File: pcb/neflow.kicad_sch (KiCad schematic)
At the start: 6 parts, among them Q1 IRLML2502, U1 MAX31855SASA, U2 MAX31855SASA, U3 LM1117DT-3.3

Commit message: WIP: Schematic rev0 almost done
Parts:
- added Brd1: SSD1306, SSD1306:128x64OLED, symbol SSD1306-128x64_OLED:SSD1306
- added C10, C12, C13, C2, C3, C5, C6, C7, C8, C9: 10uF, symbol Device:C_Small
- added C11: 100nF, symbol Device:C_Polarized_Small
- added C4: 10nF, symbol Device:C_Small
- added D1, D2, D3: 1N4148W, symbol Device:D_Small
- added FB2, FB3, FB4: BLM18PG471, Resistor_SMD:R_0603_1608Metric, symbol Device:FerriteBead_Small
- added J1, J2, J5: Conn_01x02_Socket, symbol Connector:Conn_01x02_Socket
- added J3: SSR0, symbol Connector:Conn_01x02_Socket
- added J4: SSR1, symbol Connector:Conn_01x02_Socket
- added J7: FAN1, symbol Connector:Conn_01x02_Socket
- added J8: FAN0, symbol Connector:Conn_01x02_Socket
- added JP1: VSel0, symbol Jumper:SolderJumper_3_Open
- added JP2: SolderJumper_3_Open, symbol Jumper:SolderJumper_3_Open
- added LS1: Speaker, symbol Device:Speaker
- added PS1: HLK-PM01, Converter_ACDC:Converter_ACDC_HiLink_HLK-PMxx, symbol Converter_ACDC:HLK-PM01
- added Q2, Q3, Q4, Q5: IRLML2502, Package_TO_SOT_SMD:SOT-23, symbol Transistor_FET:IRLML2060
- added R1: R_Small, symbol Device:R_Small
- added R10, R2, R3, R4, R5, R6, R7, R8, R9: 10K, symbol Device:R_Small
- added SW1, SW2, SW3, SW4: SW_Push, symbol Switch:SW_Push
- C1: value 0.01uF -> 10nF; LCSC (none) -> C57112
- FB1: LCSC (none) -> C97853
- Q1: LCSC (none) -> C2589
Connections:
- net GND: now reaches U3.1 (GND)
- net GND: now also Q1.2 (S), U1.1 (GND), U2.1 (GND), Brd1.1 (GND), C10.2, C11.2, C12.2, C13.2, C2.2, C3.2, C5.2, C6.2, C7.2, C8.2, C9.2, JP1.3 (B), JP2.3 (B), Q2.2 (S), Q3.2 (S), Q4.2 (S), Q5.2 (S), R2.1, R3.1, R4.1, R5.1, R6.1, SW1.1, SW2.1, SW3.1, SW4.1
- net +3.3V: now reaches U3.2 (VO)
- net +3.3V: now also U1.4 (V_CC), U2.4 (V_CC), Brd1.2 (VCC), C13.1, C2.1, C3.1, C5.1, C6.1, C7.1, C8.1, D3.1 (K), LS1.1, R10.2, R7.2, R8.2, R9.2
- net +5V: now reaches U3.3 (VI)
- net +5V: now also C10.1, C11.1, C12.1, C9.1, D1.1 (K), D2.1 (K), J3.1 (Pin_1), J4.1 (Pin_1), J7.1 (Pin_1), J8.1 (Pin_1), JP1.1 (A), JP2.1 (A)
- net TC1-: now reaches U2.2 (T-)
- net TC1-: now also C4.2, FB4.2
- net TC1+: now reaches U2.3 (T+)
- net TC1+: now also C4.1, FB3.1
- net SSR0: now reaches Q1.1 (G)
- net SSR0: now also R2.2
- net SSR0B: now reaches Q1.3 (D)
- net SSR0B: now also J3.2 (Pin_2)
- net TC0+: now reaches C1.1
- net TC0+: now also U1.3 (T+), FB2.1
- net TC0-: now reaches C1.2
- net TC0-: now also FB1.2, U1.2 (T-)
- net T0-: now reaches FB1.1
- net T0-: now also J1.1 (Pin_1)
- new net: J5.1 (Pin_1), PS1.1 (AC/L)
- new net: J5.2 (Pin_2), PS1.2 (AC/N)
- new net: JP2.2 (C), PS1.3 (-Vout)
- new net: JP1.2 (C), PS1.4 (+Vout)
- new net BTN0: R7.1, SW1.2
- new net BTN1: R8.1, SW2.2
- new net BTN2: R9.1, SW3.2
- new net BTN3: R10.1, SW4.2
- new net FAN0: Q4.1 (G), R5.2
- new net FAN0B: D1.2 (A), J8.2 (Pin_2), Q4.3 (D)
- new net FAN1: Q3.1 (G), R4.2
- new net FAN1B: D2.2 (A), J7.2 (Pin_2), Q3.3 (D)
- new net SPK: Q5.1 (G), R6.2
- new net SPKB: D3.2 (A), LS1.2, Q5.3 (D)
- new net SSR1: Q2.1 (G), R3.2
- new net SSR1B: J4.2 (Pin_2), Q2.3 (D)
- new net T0+: FB2.2, J1.2 (Pin_2)
- new net T1+: FB3.2, J2.2 (Pin_2)
- new net T1-: FB4.1, J2.1 (Pin_1)
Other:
- note added: "3.3V Power Supply"
- note added: "Power Supply: AC -> 5v"
- moved on the sheet: C1, FB1, Q1, U1, U3

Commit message: WIP: Adding button footprint
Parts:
- LS1: footprint (none) -> Library:PassiveBuzzerSMD_JiangsuHuaneng_MLT-5030
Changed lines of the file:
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@@
       (effects (font (size 1.27 1.27)) (justify left))
     )
-    (property "Footprint" "" (at 198.12 157.48 0)
+    (property "Footprint" "Library:PassiveBuzzerSMD_JiangsuHuaneng_MLT-5030" (at 198.12 157.48 0)
       (effects (font (size 1.27 1.27)) hide)
     )

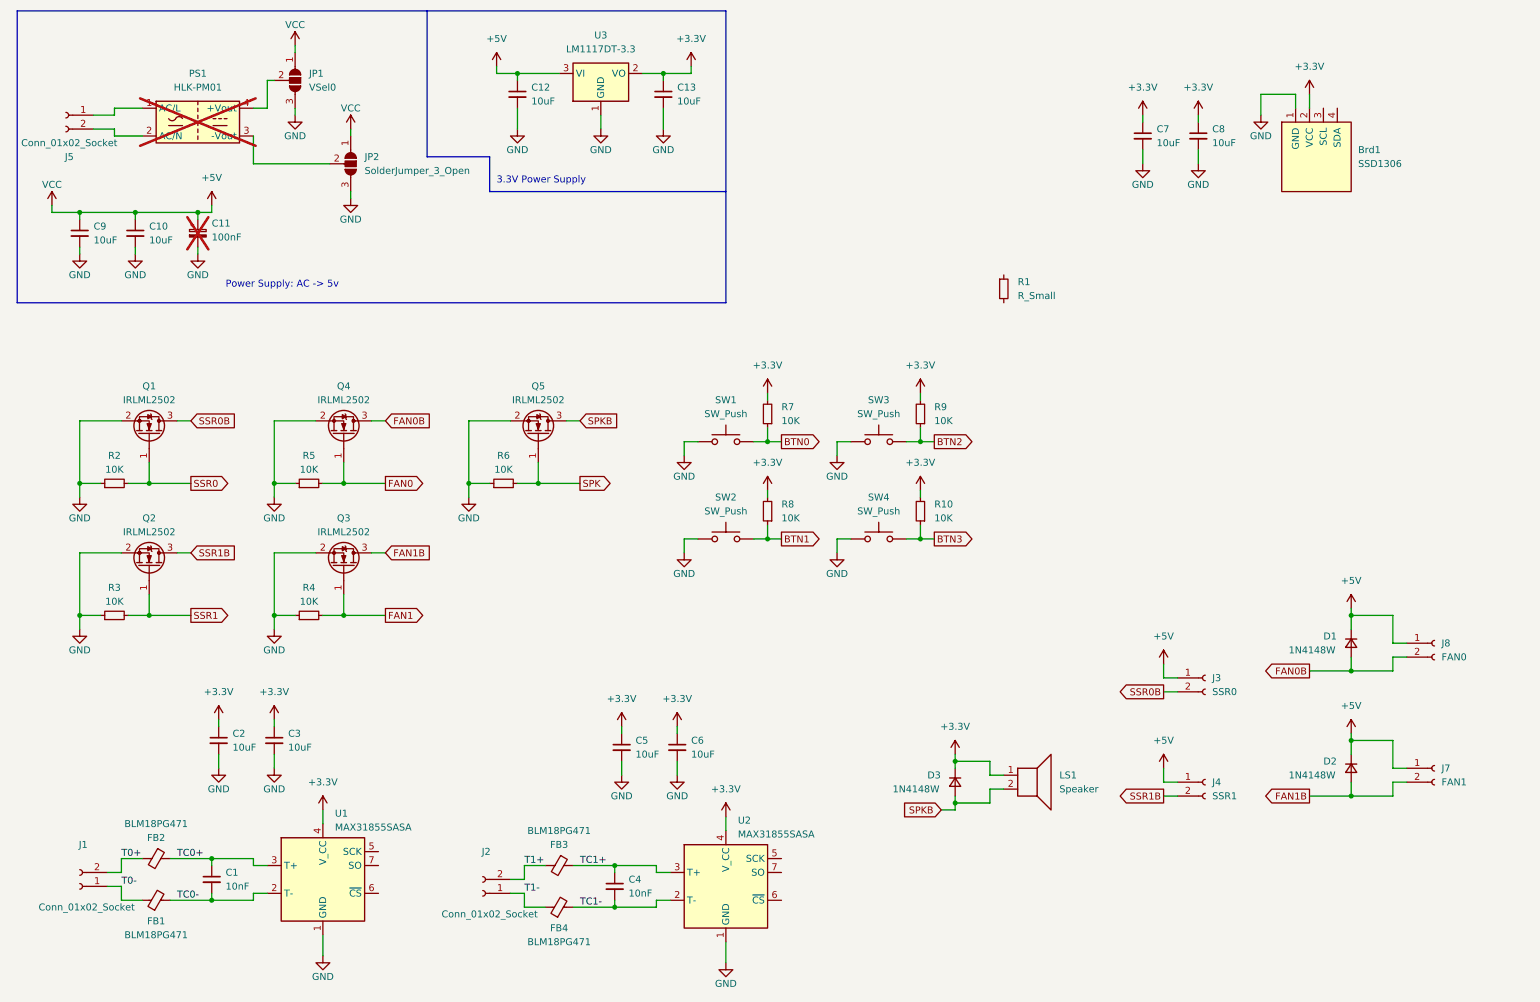
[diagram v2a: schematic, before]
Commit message: Feature/code refactor (#1)
* Starting to split screens in appropriate sections and files

* Pushing notes

* WIP: switching to laptop

* Basic new flow for cleanup structure

* Add silicone_btn and pcb

* WIP: Finished new profiles menu

* WIP: Adding new edit screen base

* WIP: additing value edit arrows

* WIP: Editing value

* WIP: added back button to the new edit screen

* Adding almost finished schematic

* Added power to pico

* WIP: Switching to workstation

* WIP: Working on pcb

* WIP: changes to pcb

* WIP: Finishing the pcb rev0

* WIP: Switching workstation

* Code changes

* WIP: Switching to desktop

* WIP: Sleepy time

* WIP: Edit menu now uses profile values, time decrease logic added

* WIP: Added config edit screen base

* Added config screen and saving to flash of the config screen

* Extended memory system and added clearing function to test menu

* Finishing memory system bugs:

* Profile screen memory fixes

* Adding profile saving

* WIP: Working on tempsystem

* Working on temp system

* Implemented quick pid and cleaned up the tempsys

* WIP: Begining code cleanup

* WIP: Cleaning up some warnings and some more menu code

* WIP: Cleaned up the nf_menu and nf_config

* WIP: Added todo comment for next time

* Adding graph and tuning tempsys

* WIP: Crude graph drawing added

* WIP: Working on calibration

* Reworking the graph system

* Fixed saving bug added dash line

* WIP stashing changes

* WIP: Switching workstations

* WIP: Switching back

* WIP: Stashing

* WIP: Stashing code switching workstation

* WIP: Stashing code

* WIP: switching workstation

* WIP: Finishing up for the weekend

* Finishing up the profile run code

* Editing todo.md

* First reflow its a start

* Adding back button and fixing temprature bugs

* Added TLV803E supply voltage supervisor

* Adding new pcb changes for v2 pcb with reset logic

* Removing old TO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
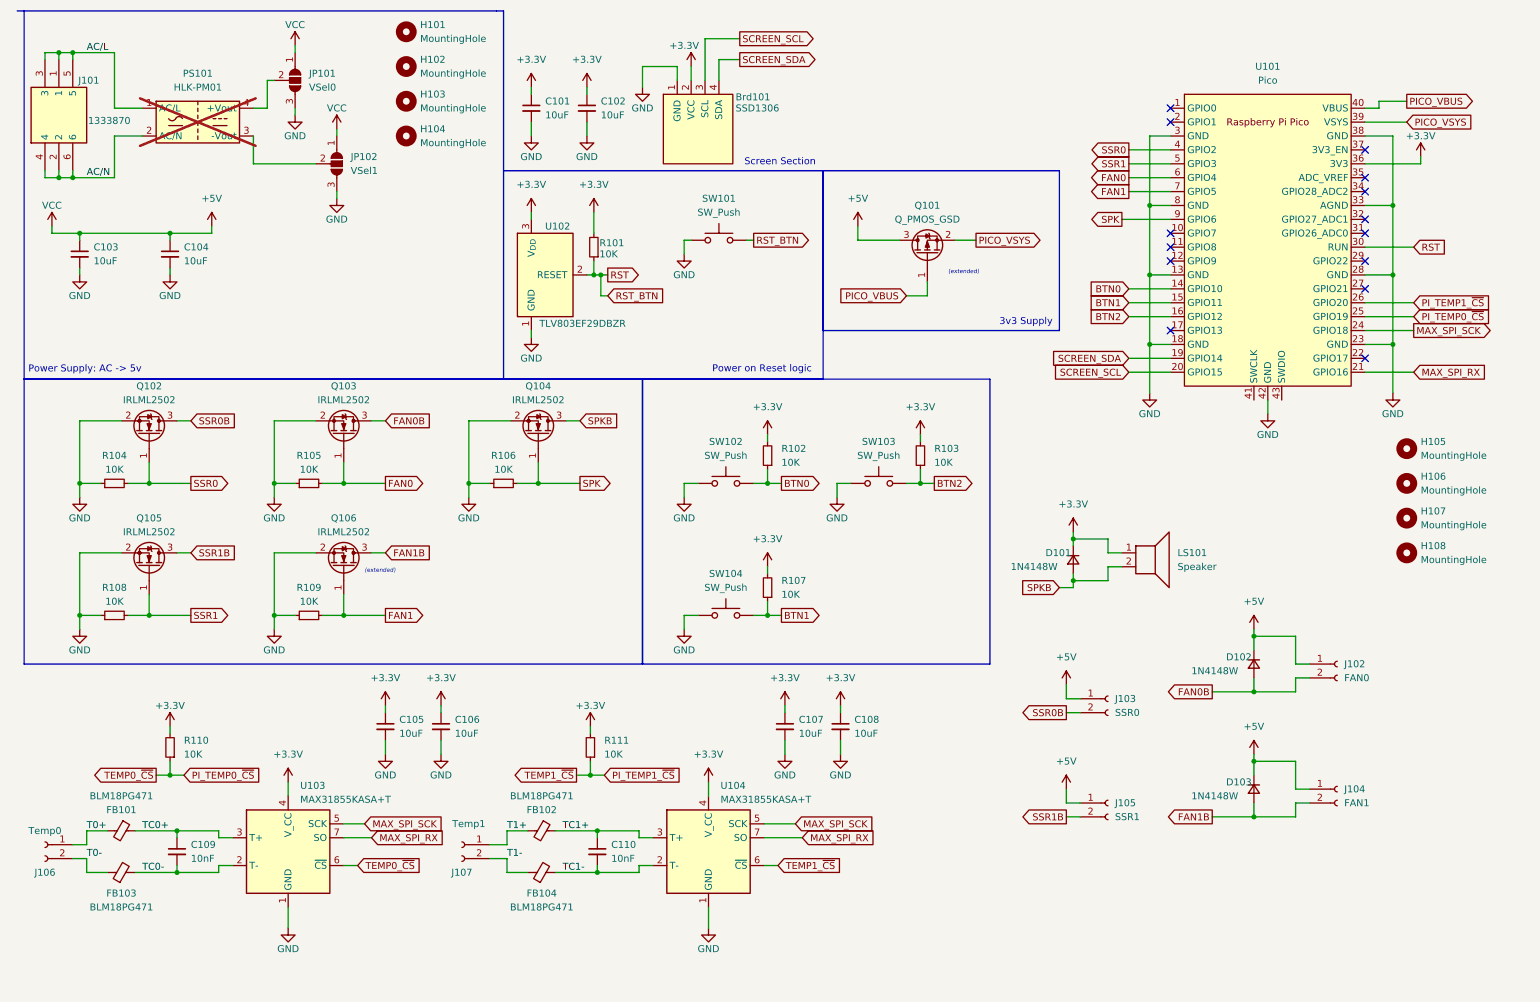
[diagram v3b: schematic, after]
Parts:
- removed C11: 100nF, symbol Device:C_Polarized_Small
- removed C12, C13: 10uF, symbol Device:C_Small
- removed J5: Conn_01x02_Socket, symbol Connector:Conn_01x02_Socket
- removed R1: R_Small, symbol Device:R_Small
- removed R10: 10K, symbol Device:R_Small
- removed SW4: SW_Push, symbol Switch:SW_Push
- removed U3: LM1117DT-3.3, Package_TO_SOT_SMD:TO-252-3_TabPin2, symbol Regulator_Linear:LM1117DT-3.3
- added H101, H102, H103, H104, H105, H106, H107, H108: MountingHole, MountingHole:MountingHole_3mm, symbol Mechanical:MountingHole
- added J101: 1333870, Unshareable:1333870, symbol 1333870:1333870
- added Q101: Q_PMOS_GSD, Package_TO_SOT_SMD:SOT-23, symbol Device:Q_PMOS_GSD
- added R101, R110, R111: 10K, Resistor_SMD:R_0603_1608Metric, symbol Device:R_Small
- added SW101: SW_Push, silicone_btn:BUTTON_SILICON, symbol Switch:SW_Push
- added U101: Pico, MCU_RaspberryPi_and_Boards:RPi_Pico_SMD_TH, symbol MCU_RaspberryPi_and_Boards:Pico
- added U102: TLV803EF29DBZR, Package_TO_SOT_SMD:SOT-23, symbol Power_Supervisor:TLV810EA29DBZ
- Brd101: renamed from Brd1; now left out of the parts list
- C101: renamed from C7; footprint (none) -> Resistor_SMD:R_0603_1608Metric
- C102: renamed from C8; footprint (none) -> Resistor_SMD:R_0603_1608Metric
- C103: renamed from C9; footprint (none) -> Resistor_SMD:R_0603_1608Metric
- C104: renamed from C10; footprint (none) -> Resistor_SMD:R_0603_1608Metric
- C105: renamed from C2; footprint (none) -> Resistor_SMD:R_0603_1608Metric
- C106: renamed from C3; footprint (none) -> Resistor_SMD:R_0603_1608Metric
- C107: renamed from C5; footprint (none) -> Resistor_SMD:R_0603_1608Metric
- C108: renamed from C6; footprint (none) -> Resistor_SMD:R_0603_1608Metric
- C109: renamed from C1; footprint (none) -> Resistor_SMD:R_0603_1608Metric
- C110: renamed from C4; footprint (none) -> Resistor_SMD:R_0603_1608Metric
- D101: renamed from D3; footprint (none) -> Diode_SMD:D_SOD-123
- D102: renamed from D1; footprint (none) -> Diode_SMD:D_SOD-123
- D103: renamed from D2; footprint (none) -> Diode_SMD:D_SOD-123
- J102: renamed from J8; footprint (none) -> Connector_JST:JST_XH_B2B-XH-AM_1x02_P2.50mm_Vertical
- J103: renamed from J3; footprint (none) -> Connector_JST:JST_XH_B2B-XH-AM_1x02_P2.50mm_Vertical
- J104: renamed from J7; footprint (none) -> Connector_JST:JST_XH_B2B-XH-AM_1x02_P2.50mm_Vertical
- J105: renamed from J4; footprint (none) -> Connector_JST:JST_XH_B2B-XH-AM_1x02_P2.50mm_Vertical
- J106: renamed from J1; value Conn_01x02_Socket -> Temp0; footprint (none) -> Connector_JST:JST_XH_B2B-XH-AM_1x02_P2.50mm_Vertical
- J107: renamed from J2; value Conn_01x02_Socket -> Temp1; footprint (none) -> Connector_JST:JST_XH_B2B-XH-AM_1x02_P2.50mm_Vertical
- JP101: renamed from JP1; footprint (none) -> Jumper:SolderJumper-3_P1.3mm_Open_Pad1.0x1.5mm
- JP102: renamed from JP2; value SolderJumper_3_Open -> VSel1; footprint (none) -> Jumper:SolderJumper-3_P1.3mm_Open_Pad1.0x1.5mm
- LS101: renamed from LS1; now left out of the parts list
- PS101: renamed from PS1; now left out of the parts list
- R102: renamed from R7; footprint (none) -> Resistor_SMD:R_0603_1608Metric
- R103: renamed from R9; footprint (none) -> Resistor_SMD:R_0603_1608Metric
- R104: renamed from R2; footprint (none) -> Resistor_SMD:R_0603_1608Metric
- R105: renamed from R5; footprint (none) -> Resistor_SMD:R_0603_1608Metric
- R106: renamed from R6; footprint (none) -> Resistor_SMD:R_0603_1608Metric
- R107: renamed from R8; footprint (none) -> Resistor_SMD:R_0603_1608Metric
- R108: renamed from R3; footprint (none) -> Resistor_SMD:R_0603_1608Metric
- R109: renamed from R4; footprint (none) -> Resistor_SMD:R_0603_1608Metric
- SW102: renamed from SW1; footprint (none) -> silicone_btn:BUTTON_SILICON; now left out of the parts list
- SW103: renamed from SW3; footprint (none) -> silicone_btn:BUTTON_SILICON; now left out of the parts list
- SW104: renamed from SW2; footprint (none) -> silicone_btn:BUTTON_SILICON; now left out of the parts list
- U103: renamed from U1; value MAX31855SASA -> MAX31855KASA+T; LCSC (none) -> C52028
- U104: renamed from U2; value MAX31855SASA -> MAX31855KASA+T; LCSC (none) -> C52028
- renumbered FB2 to FB101, FB3 to FB102, FB1 to FB103, FB4 to FB104, Q1 to Q102, Q4 to Q103, Q5 to Q104, Q2 to Q105, Q3 to Q106
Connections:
- net +3.3V: now also R101.2, R110.2, R111.2, U101.36 (3V3), U102.3 (V_{DD})
- net +5V: now also Q101.3 (D)
- net BTN0: now also U101.14 (GPIO10)
- net BTN1: now also U101.15 (GPIO11)
- net BTN2: now also U101.16 (GPIO12)
- net FAN0: now also U101.6 (GPIO4)
- net FAN1: now also U101.7 (GPIO5)
- net GND: now also SW101.1, U101.13 (GND), U101.18 (GND), U101.23 (GND), U101.28 (GND), U101.3 (GND), U101.33 (AGND), U101.38 (GND), U101.42 (GND), U101.8 (GND), U102.1 (GND)
- net SPK: now also U101.9 (GPIO6)
- net SSR0: now also U101.4 (GPIO2)
- net SSR1: now also U101.5 (GPIO3)
- net T0+: now also J106.1 (Pin_1); no longer J106.2 (Pin_2)
- net T0-: now also J106.2 (Pin_2); no longer J106.1 (Pin_1)
- net T1+: now also J107.1 (Pin_1); no longer J107.2 (Pin_2)
- net T1-: now also J107.2 (Pin_2); no longer J107.1 (Pin_1)
- net AC/L: now reaches PS101.1 (AC/L)
- net AC/L: now also J101.1, J101.3, J101.5
- net AC/N: now reaches PS101.2 (AC/N)
- net AC/N: now also J101.2, J101.4, J101.6
- net SCREEN_SCL: now reaches Brd101.3 (SCL)
- net SCREEN_SCL: now also U101.20 (GPIO15)
- net SCREEN_SDA: now reaches Brd101.4 (SDA)
- net SCREEN_SDA: now also U101.19 (GPIO14)
- net MAX_SPI_SCK: now reaches U103.5 (SCK)
- net MAX_SPI_SCK: now also U104.5 (SCK), U101.24 (GPIO18)
- net PI_TEMP0_~{CS}: now reaches U103.6 (~{CS})
- net PI_TEMP0_~{CS}: now also R110.1, U101.25 (GPIO19)
- net MAX_SPI_RX: now reaches U103.7 (SO)
- net MAX_SPI_RX: now also U104.7 (SO), U101.21 (GPIO16)
- net PI_TEMP1_~{CS}: now reaches U104.6 (~{CS})
- net PI_TEMP1_~{CS}: now also R111.1, U101.26 (GPIO20)
- new net PICO_VBUS: Q101.1 (G), U101.40 (VBUS)
- new net PICO_VSYS: Q101.2 (S), U101.39 (VSYS)
- new net RST: R101.1, SW101.2, U101.30 (RUN), U102.2 (RESET)
- no-connect marks 0 -> 14
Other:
- note added: "(extended)"
- note added: "3v3 Supply"
- note added: "Power on Reset logic"
- note added: "Screen Section"
- note removed: "3.3V Power Supply"
- moved on the sheet: Brd101, C101, C102, C103, C104, C105, C106, C107, C108, C109, C110, D101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
